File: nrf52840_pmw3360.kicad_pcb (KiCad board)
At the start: 2 copper layers, 18 x 33 mm, 3 parts, among them J1 PMW3360_Connector, J2 Battery_JST-PH, U1 SuperMini_nRF52840

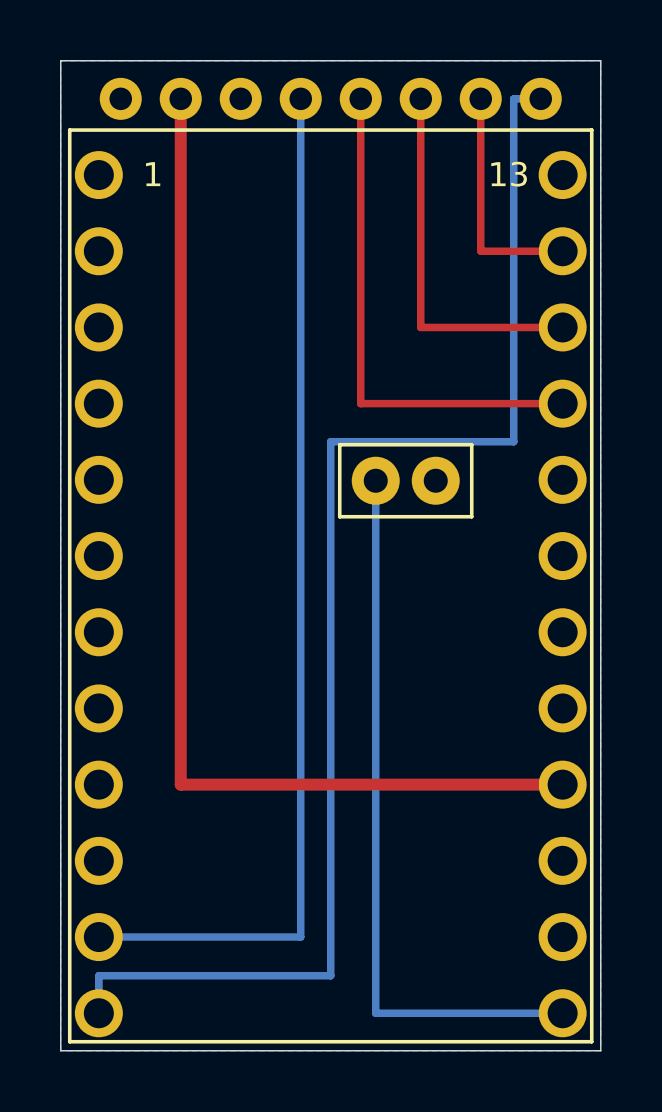
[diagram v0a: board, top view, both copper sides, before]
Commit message: fix: GNDパッド間をB.Cuトレースで明示接続（ゾーンフィル非依存）
Co-Authored-By: Claude Sonnet 4.6 <noreply@anthropic.com>
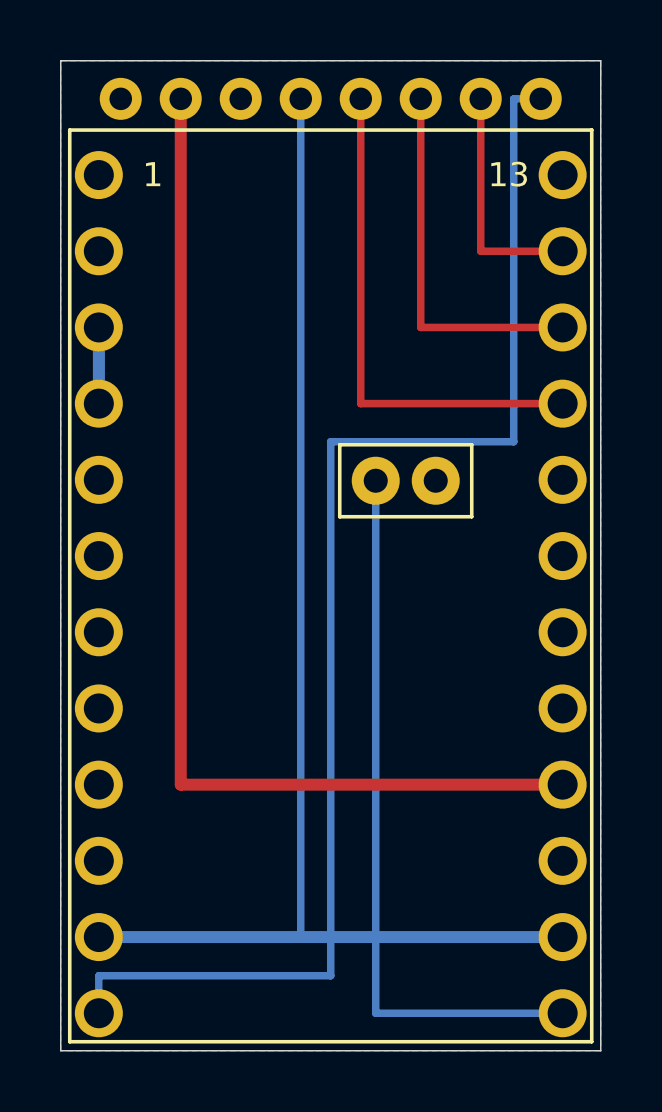
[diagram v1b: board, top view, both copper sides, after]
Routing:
- net GND: track 0.00 -> 18.0 mm
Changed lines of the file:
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@@
 (segment (start 143.0000 86.2700) (end 143.0000 114.2100) (width 0.2500) (layer "B.Cu") (net 7))
 (segment (start 143.0000 114.2100) (end 136.2700 114.2100) (width 0.2500) (layer "B.Cu") (net 7))
+(segment (start 136.2700 93.8900) (end 136.2700 96.4300) (width 0.4000) (layer "B.Cu") (net 1))
+(segment (start 151.7300 114.2100) (end 136.2700 114.2100) (width 0.4000) (layer "B.Cu") (net 1))
 (zone (net 1) (net_name "GND") (layer "B.Cu")
   (hatch edge 0.508)

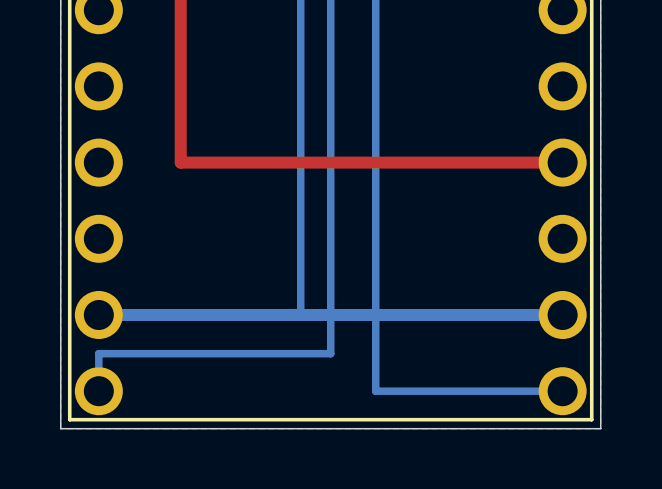
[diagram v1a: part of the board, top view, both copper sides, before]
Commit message: fix: B.Cu交差エラー5件修正（誤ったGND水平トレース削除）
Co-Authored-By: Claude Sonnet 4.6 <noreply@anthropic.com>
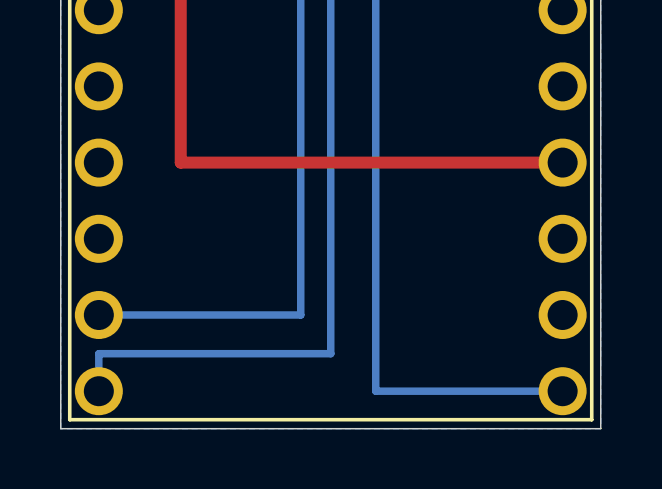
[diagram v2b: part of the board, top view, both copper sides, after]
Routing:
- net GND: track 18.0 -> 2.54 mm
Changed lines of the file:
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@@
 (segment (start 143.0000 114.2100) (end 136.2700 114.2100) (width 0.2500) (layer "B.Cu") (net 7))
 (segment (start 136.2700 93.8900) (end 136.2700 96.4300) (width 0.4000) (layer "B.Cu") (net 1))
-(segment (start 151.7300 114.2100) (end 136.2700 114.2100) (width 0.4000) (layer "B.Cu") (net 1))
 (zone (net 1) (net_name "GND") (layer "B.Cu")
   (hatch edge 0.508)

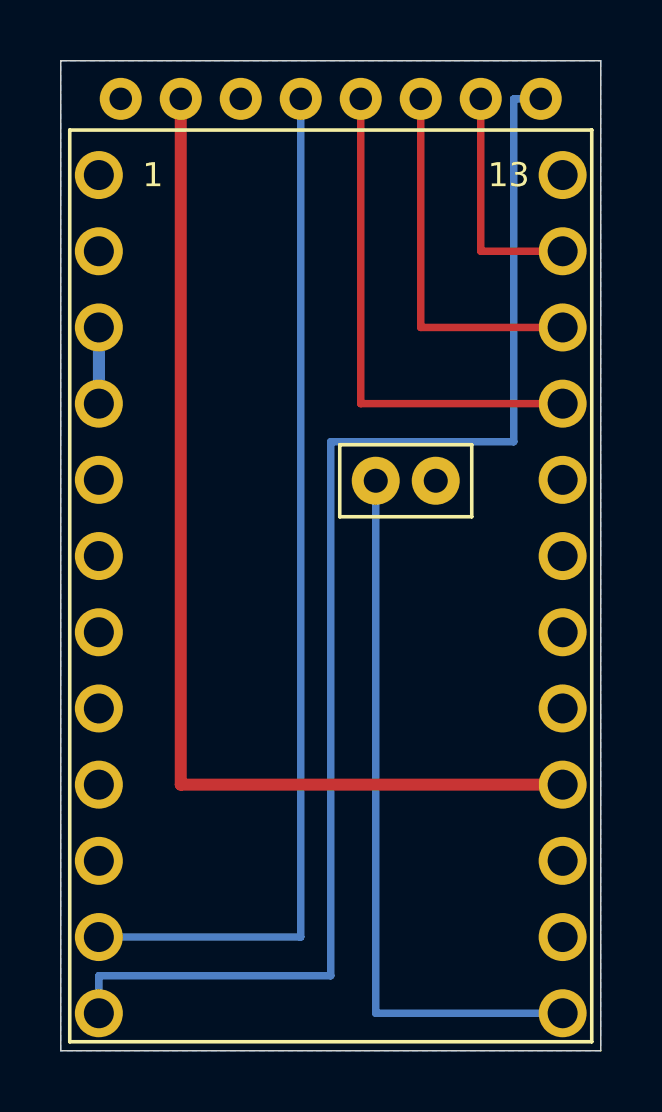
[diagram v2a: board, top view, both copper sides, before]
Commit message: fix: GNDゾーン削除→F.Cu明示トレースで全GNDパッドを接続（ゾーン孤立島問題を根本解決）
Co-Authored-By: Claude Sonnet 4.6 <noreply@anthropic.com>
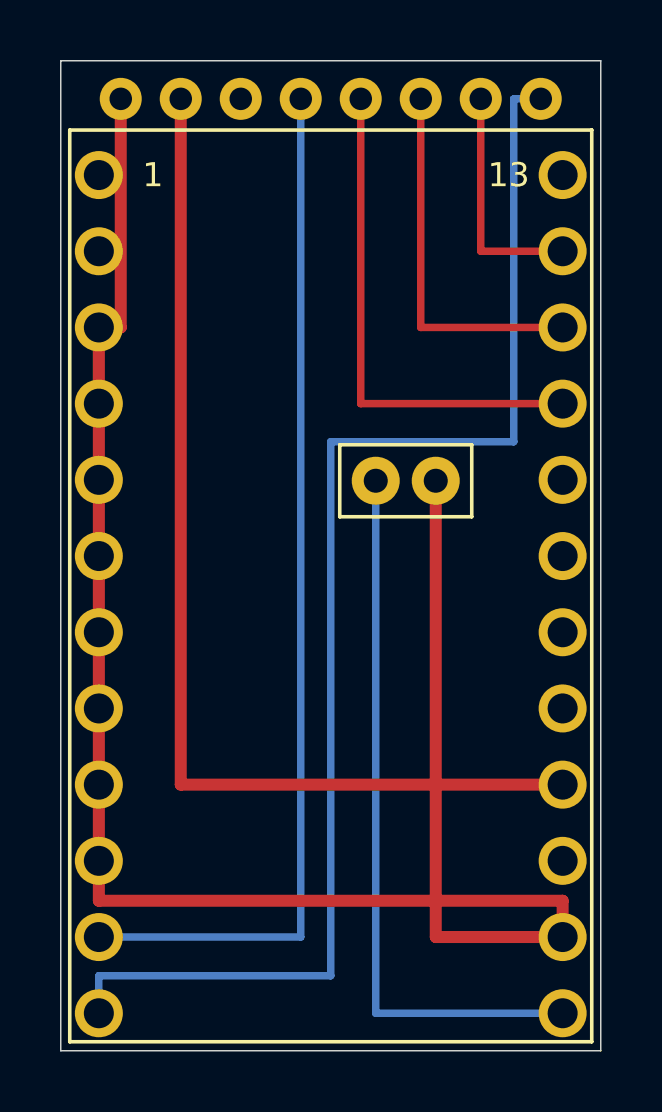
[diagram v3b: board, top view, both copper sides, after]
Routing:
- net GND: track 2.54 -> 66.1 mm
- removed copper zone on B.Cu, net GND
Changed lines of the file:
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@@
 (segment (start 143.0000 86.2700) (end 143.0000 114.2100) (width 0.2500) (layer "B.Cu") (net 7))
 (segment (start 143.0000 114.2100) (end 136.2700 114.2100) (width 0.2500) (layer "B.Cu") (net 7))
+(segment (start 137.0000 86.2700) (end 137.0000 93.8900) (width 0.4000) (layer "F.Cu") (net 1))
+(segment (start 137.0000 93.8900) (end 136.2700 93.8900) (width 0.4000) (layer "F.Cu") (net 1))
+(segment (start 136.2700 93.8900) (end 136.2700 113.0000) (width 0.4000) (layer "F.Cu") (net 1))
+(segment (start 136.2700 113.0000) (end 151.7300 113.0000) (width 0.4000) (layer "F.Cu") (net 1))
+(segment (start 151.7300 113.0000) (end 151.7300 114.2100) (width 0.4000) (layer "F.Cu") (net 1))
+(segment (start 147.5000 99.0000) (end 147.5000 114.2100) (width 0.4000) (layer "F.Cu") (net 1))
+(segment (start 147.5000 114.2100) (end 151.7300 114.2100) (width 0.4000) (layer "F.Cu") (net 1))
 (segment (start 136.2700 93.8900) (end 136.2700 96.4300) (width 0.4000) (layer "B.Cu") (net 1))
-(zone (net 1) (net_name "GND") (layer "B.Cu")
-  (hatch edge 0.508)
-  (connect_pads yes (clearance 0.2))
-  (min_thickness 0.25)
-  (filled_areas_thickness no)
-  (fill (thermal_gap 0.3) (thermal_bridge_width 0.3))
-  (polygon (pts
-    (xy 135.0000 85.0000) (xy 153.0000 85.0000)
-    (xy 153.0000 118.0000) (xy 135.0000 118.0000)))
-)
 (gr_text "nRF52840+PMW3360" (at 144.0000 116.5000 0) (layer "F.Fab")
   (effects (font (size 0.8 0.8) (thickness 0.15))))
